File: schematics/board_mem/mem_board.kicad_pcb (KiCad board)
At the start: 2 copper layers, 150.3 x 100.3 mm, 43 parts, among them J1 J101A, J10 J100B, J11 J100C, J2 BA22, J29 ramRom29, J3 ramRom3, J30 rom2Rom5_30, J31 ramRom31, J4 J100A, J5 J100A, J6 J100B, J600 Euro96pin, J7 J100C, J8 J100A, J9 J100A, U100A1 74HC138, U100B1 74HC138, U101A1 RAM_LOW, U101B1 RAM_HIGH, U102A1 RAM_LOW, U102B1 RAM_HIGH, U103A1 RAM_LOW, U103B1 RAM_HIGH, U104A1 RAM_LOW, U104B1 RAM_HIGH, U105A1 RAM_LOW, U105B1 RAM_HIGH

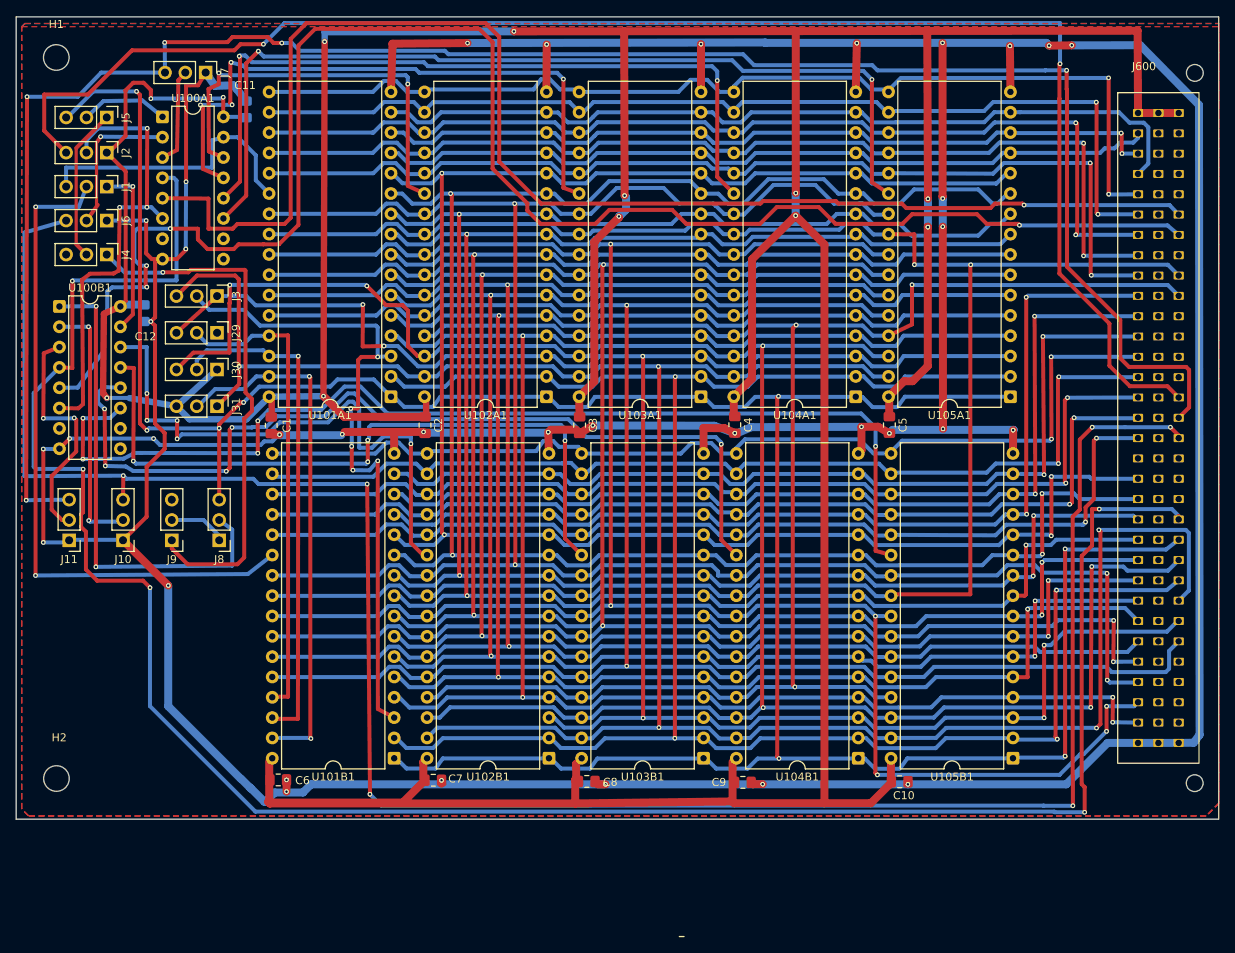
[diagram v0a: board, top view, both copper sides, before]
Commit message: Finished PDS100 routing
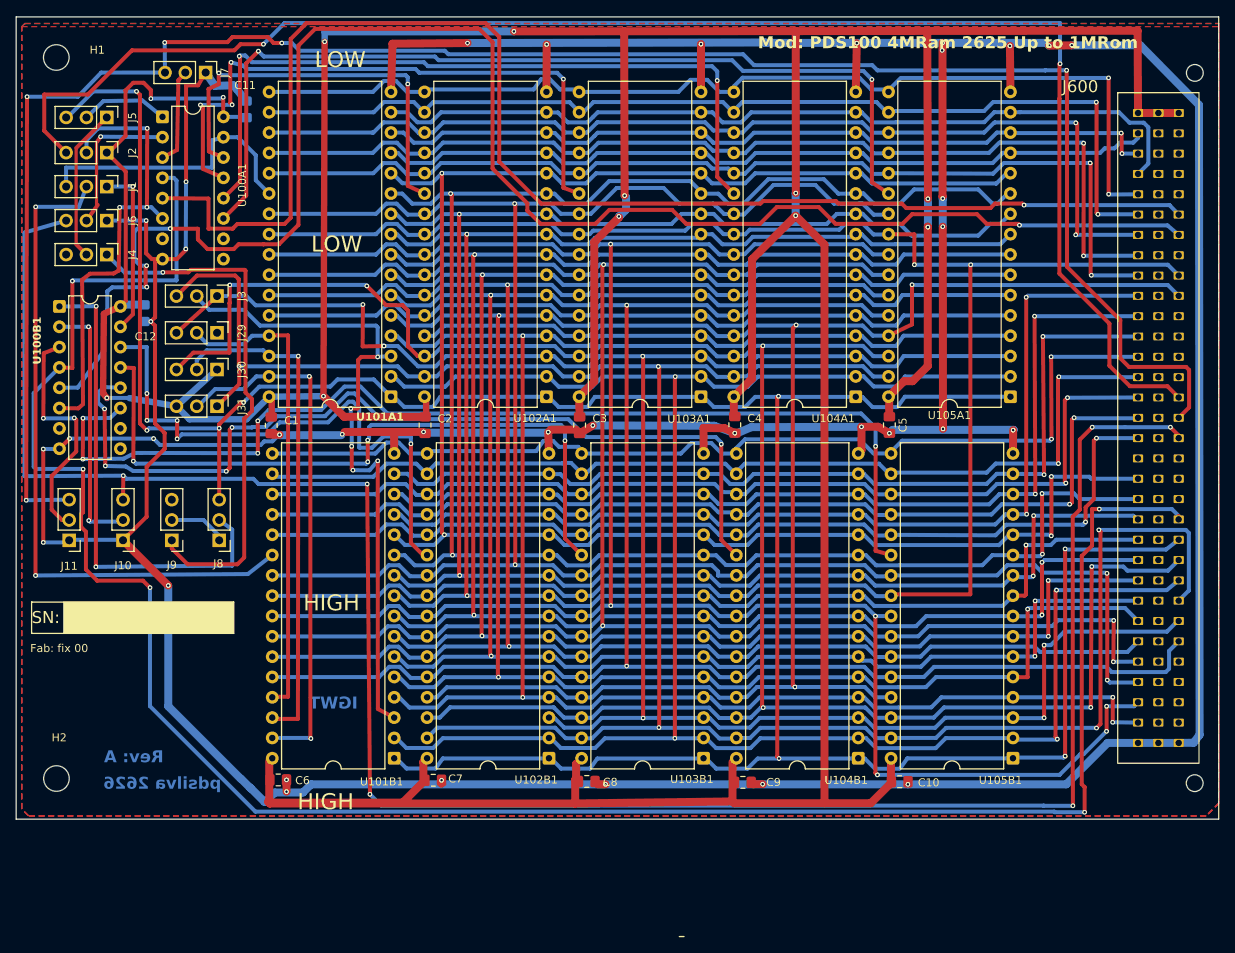
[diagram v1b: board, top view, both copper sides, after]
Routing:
- net GND: vias 35 -> 37
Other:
- board text added: "Fab: fix 00"
- board text added: "HIGH"
- board text added: "IGWT"
- board text added: "LOW"
- board text added: "Mod: PDS100 4MRam 2625 Up to 1MRom"
- board text added: "Rev: A"
- board text added: "SN:"
- board text added: "pdsilva 2626"
